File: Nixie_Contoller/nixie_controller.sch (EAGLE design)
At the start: 42 parts, among them IC1 DS1307, IC2 MAX1771ESA, IC3 7805T, J1 CON-SOCJ-2155, Q1 16MHz, T1 IRF644PBF, U1 328P, U2 HU2032-LF, X1 22-23-2021, Y2 32.768kHz

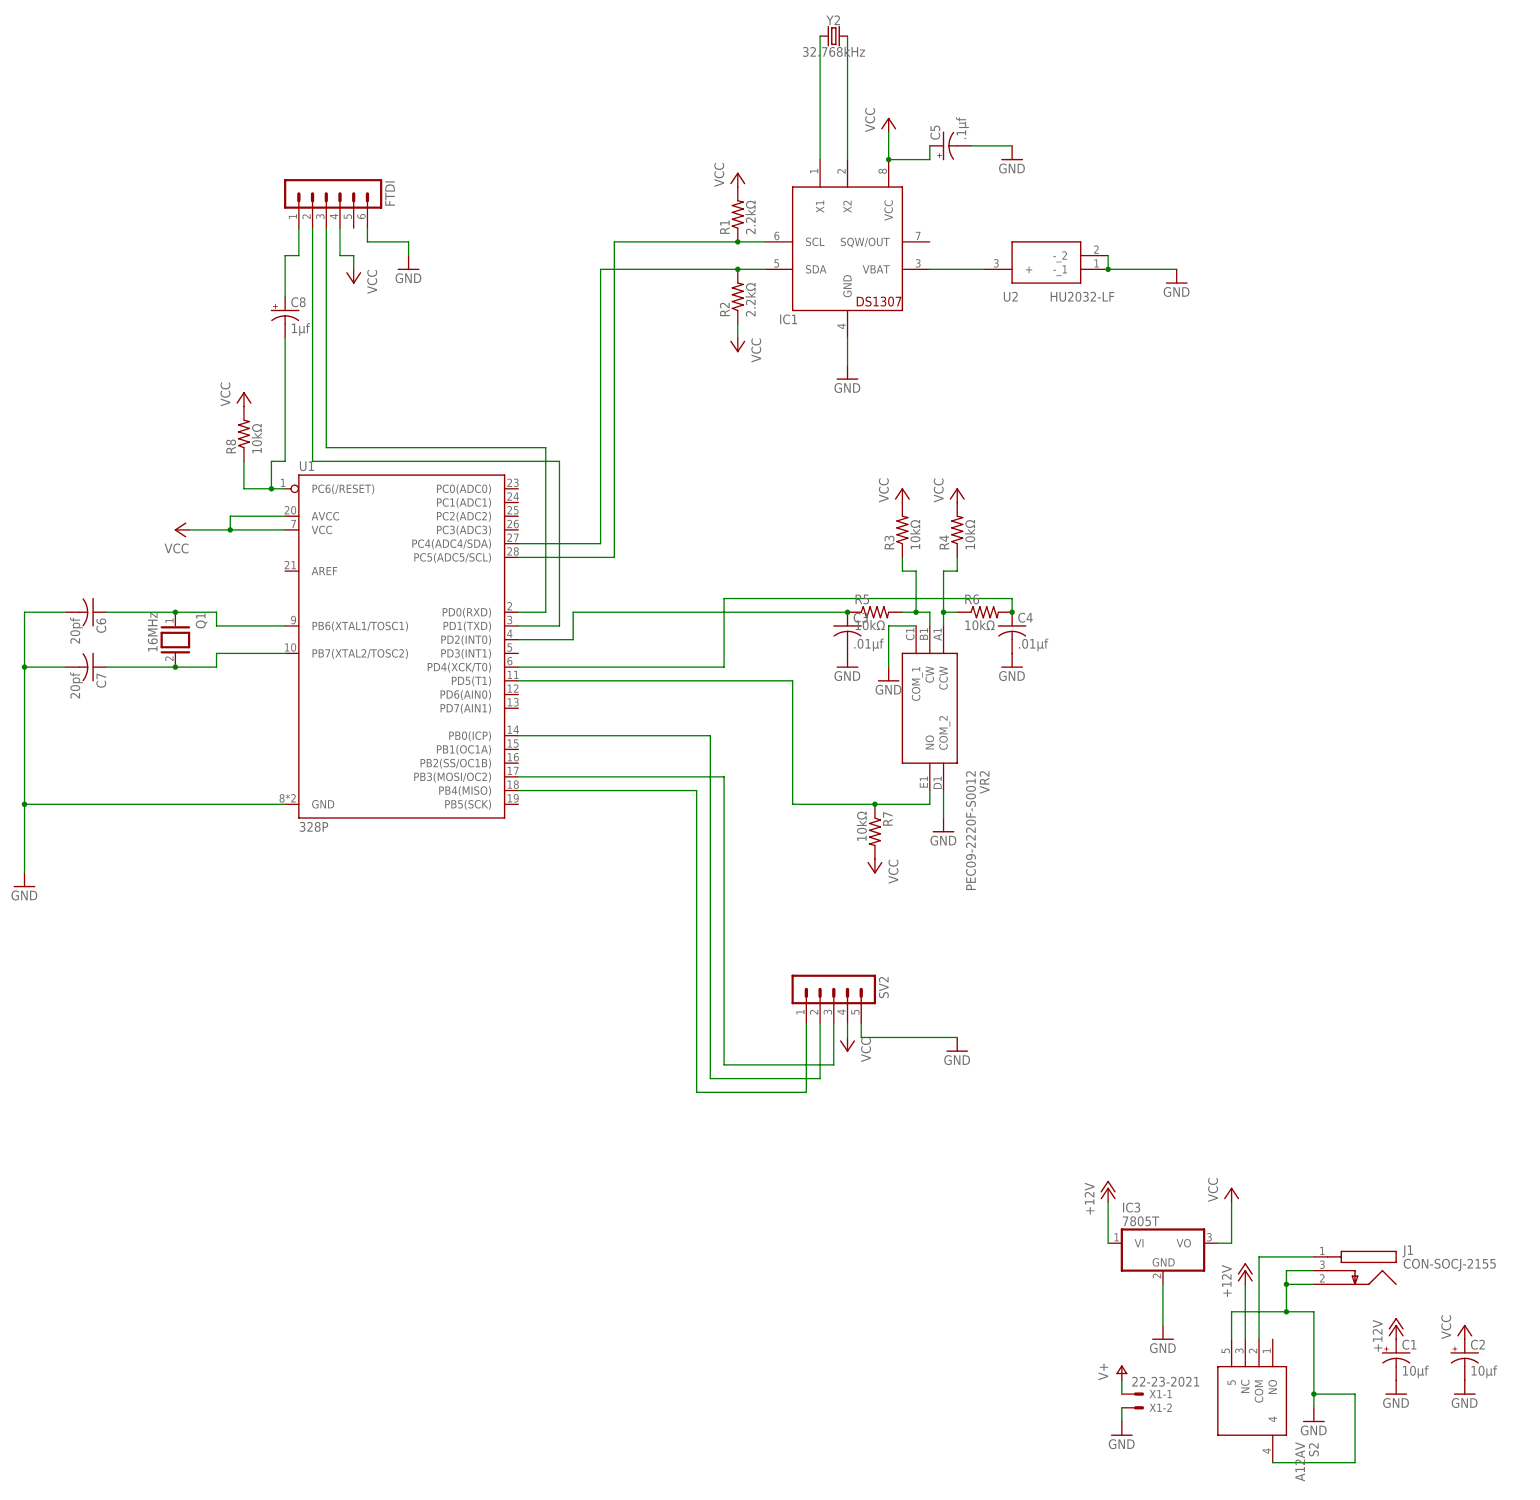
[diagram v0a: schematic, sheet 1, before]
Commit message: Updates parts to Digikey equivalent, adds BOM, adds SHDN to pin 5
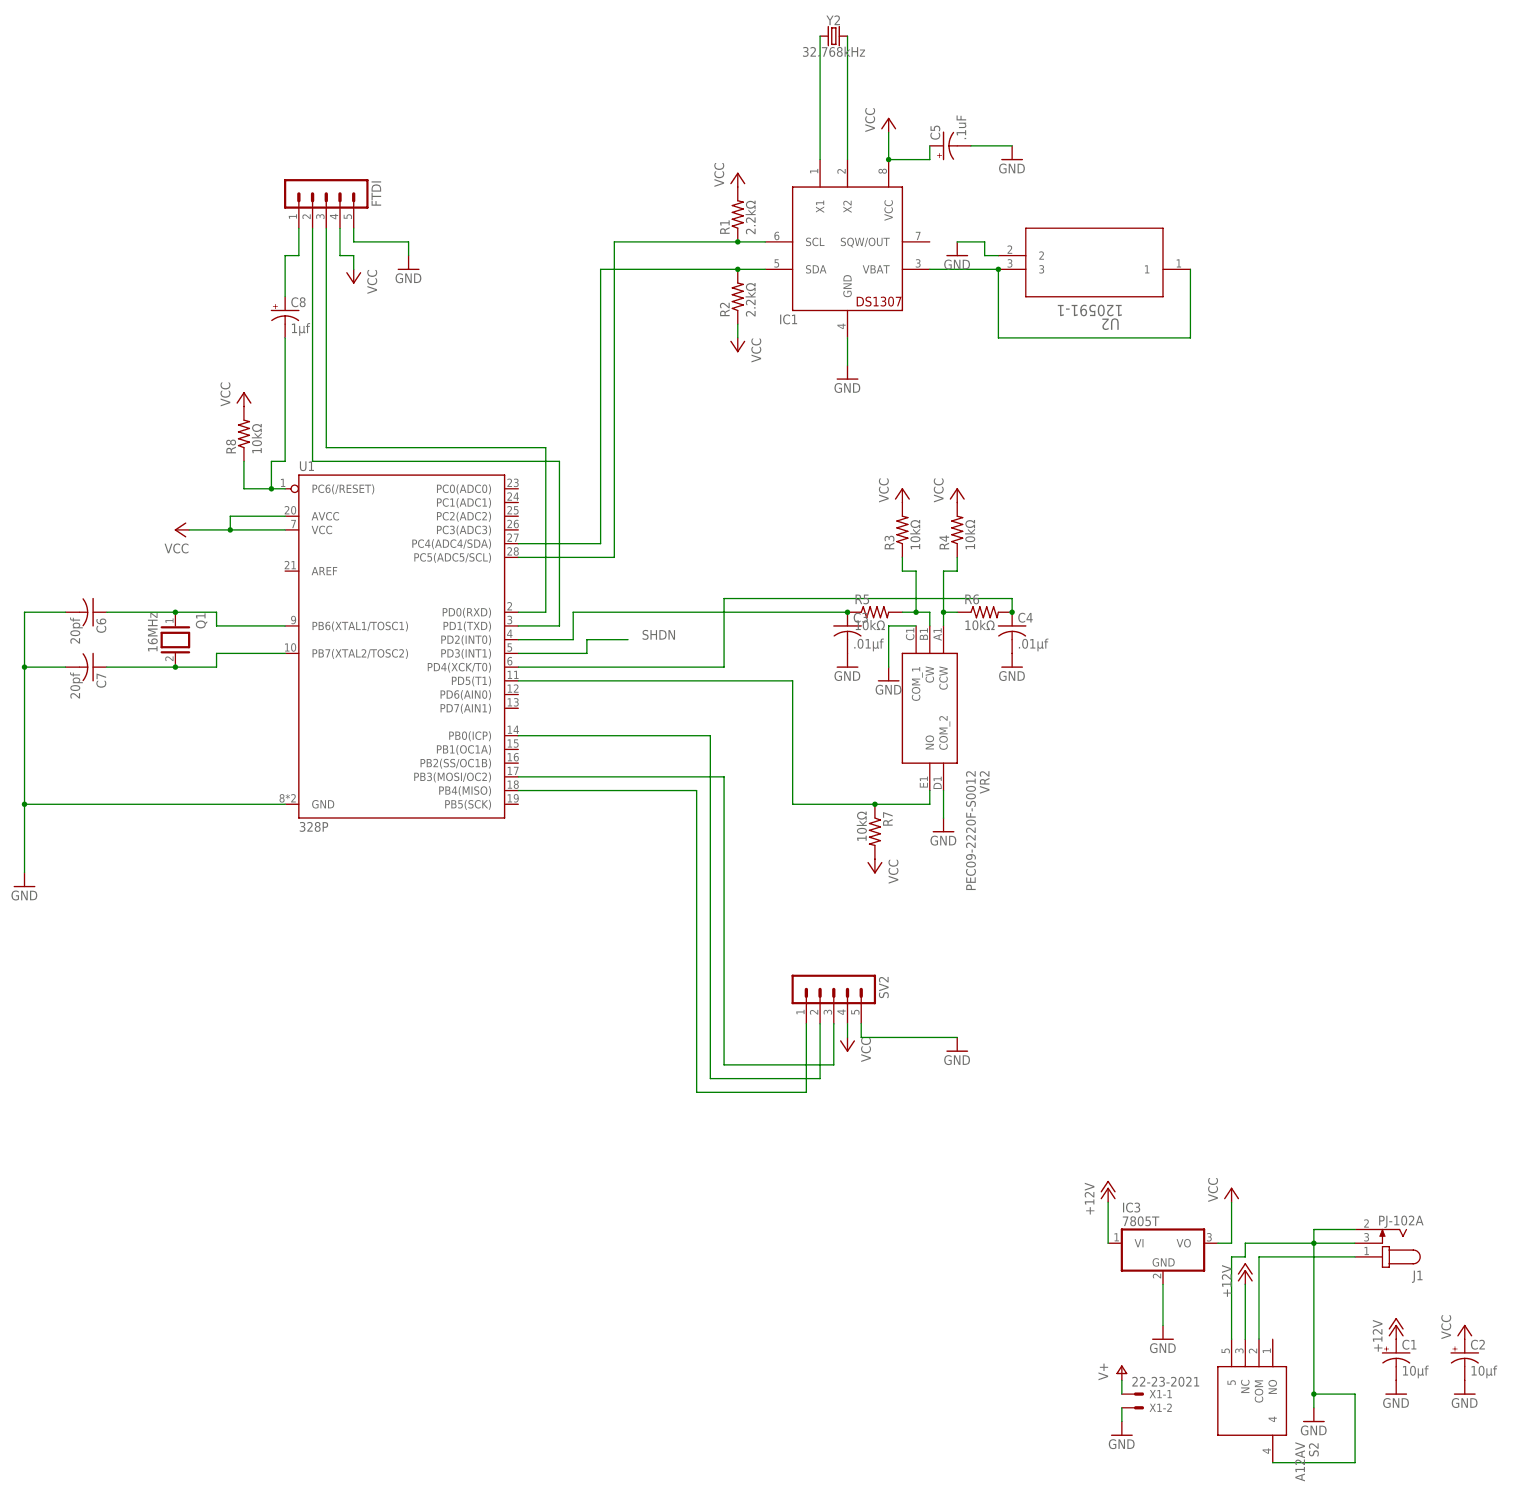
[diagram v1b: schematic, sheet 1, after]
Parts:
- added R11: 10k, rcl:R-US_M0805
- C5: value .1μf -> .1uF
- FTDI: device con-lstb:MA06-1 -> con-lstb:MA05-1
- J1: value CON-SOCJ-2155 -> PJ-102A; device SamacSys_Parts:CON-SOCJ-2155 -> PJ-102A:PJ-102A
- U2: value HU2032-LF -> 120591-1; device SamacSys_Parts:HU2032-LF -> TE Connectivity AMP Connectors 120591-1:120591-1
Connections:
- new net SHDN: IC2.SHDN, R11.2, U1.PD3(INT1)
- net +12V: now also R11.1
- net GND: now also FTDI.5, U2.2; no longer FTDI.6, IC2.SHDN, U2.-_1, U2.-_2
- net N$1: now also U2.1, U2.3; no longer U2.+
